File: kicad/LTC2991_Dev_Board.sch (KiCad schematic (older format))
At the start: 9 parts

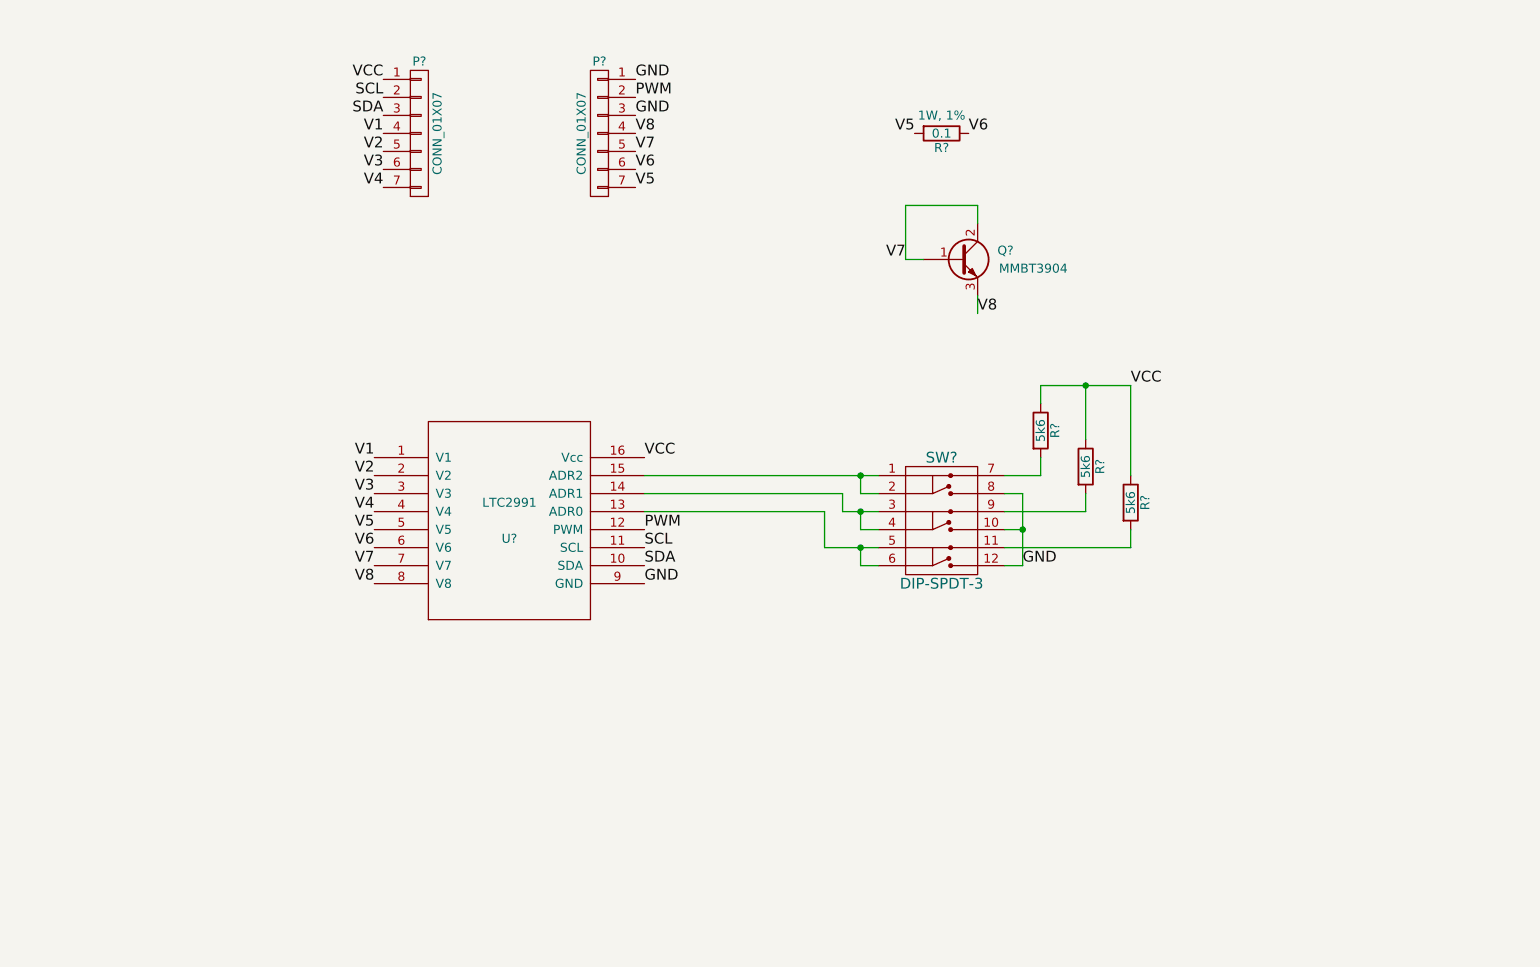
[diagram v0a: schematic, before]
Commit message: Beginning stages of PCB layout. Likely to need a few modifications to meet board size requirements.
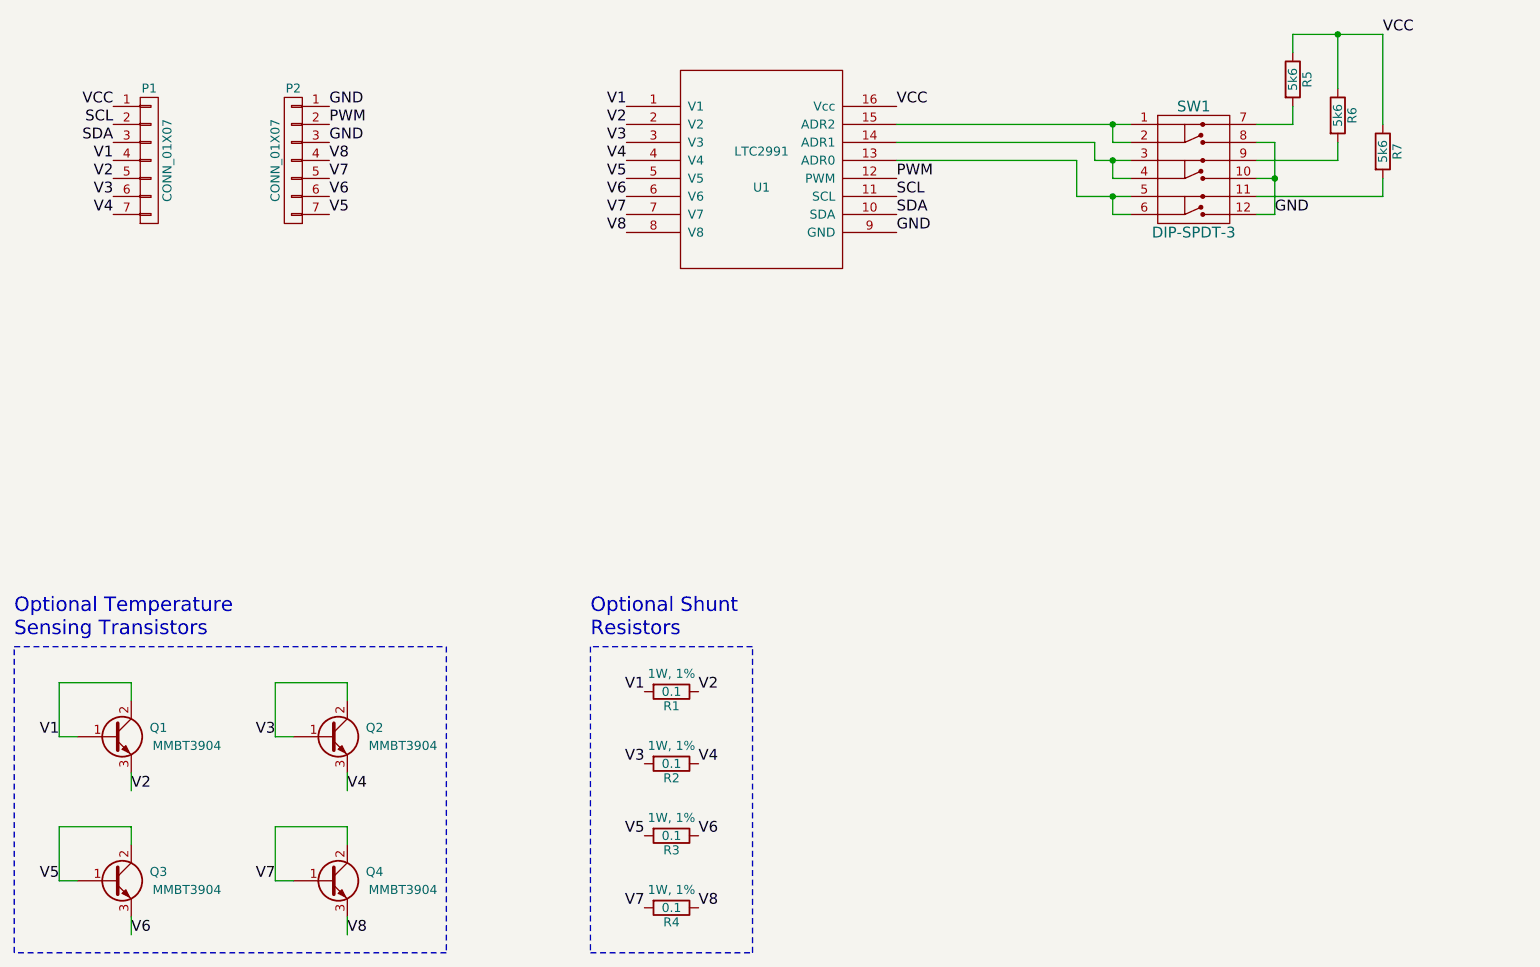
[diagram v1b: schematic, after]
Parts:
- added Q1, Q2, Q3: MMBT3904, Housings_SOT-23_SOT-143_TSOT-6:SOT-23, symbol Q_NPN_BCE
- added R2, R3, R4: 0.1, Resistors_SMD:R_2010, symbol R
- P1, P2: renamed from P?; footprint (none) -> Pin_Headers:Pin_Header_Straight_1x07
- Q4: renamed from Q?; footprint (none) -> Housings_SOT-23_SOT-143_TSOT-6:SOT-23
- R1: renamed from R?; footprint (none) -> Resistors_SMD:R_2010
- R5, R6, R7: renamed from R?; footprint (none) -> Resistors_SMD:R_1206
- SW1: renamed from SW?; footprint (none) -> Local:DIP_Switch_2x06
- U1: renamed from U?; footprint (none) -> Local:MSOP-16
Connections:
- net V1: now also R1.2, Q1.1 (B), Q1.2 (C)
- net V2: now also R1.1, Q1.3 (E)
- net V3: now also Q2.1 (B), Q2.2 (C), R2.2
- net V4: now also Q2.3 (E), R2.1
- net V5: now also Q3.1 (B), Q3.2 (C), R3.2; no longer R1.2
- net V6: now also Q3.3 (E), R3.1; no longer R1.1
- net V7: now also R4.2
- net V8: now also R4.1
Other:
- note added: "Optional Shunt\nResistors"
- note added: "Optional Temperature\nSensing Transistors"
- moved on the sheet: P1, P2, Q4, R1, R5, R6, R7, SW1, U1

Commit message: More PCB layout work, schematic tweaks. Closer to a finaly layout.
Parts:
- removed SW1: DIP-SPDT-3, Local:DIP_Switch_2x06, symbol DIP-SPDT-3
- added P3: CONN_02X03, Pin_Headers:Pin_Header_Straight_2x03, symbol CONN_02X03
- R1, R2, R3, R4: footprint Resistors_SMD:R_2010 -> Resistors_SMD:R_1206
- R5, R6, R7: footprint Resistors_SMD:R_1206 -> Resistors_SMD:R_0603
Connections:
- net GND: now also P3.1 (P1), P3.3 (P3), P3.5 (P5)
- net at U1.13 (ADR0): now also R7.2, P3.6 (P6)
- net at U1.14 (ADR1): now also R6.2, P3.4 (P4)
- net at U1.15 (ADR2): now also R5.2, P3.2 (P2)
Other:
- moved on the sheet: P1, P2, R5, R6, R7, U1
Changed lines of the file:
@@
 L LTC2991 U1
 U 1 1 55A19EC5
-P 5500 2950
-F 0 "U1" H 5500 2850 50  0000 C CNN
-F 1 "LTC2991" H 5500 3050 50  0000 C CNN
-F 2 "Local:MSOP-16" H 5500 2950 50  0001 C CNN
-F 3 "" H 5500 2950 50  0001 C CNN
-	1    5500 2950
-	1    0    0    -1
-$EndComp
-$Comp
-L DIP-SPDT-3 SW1
-U 1 1 55A1BC78
-P 7900 3200
-F 0 "SW1" H 7900 3800 60  0000 C CNN
-F 1 "DIP-SPDT-3" H 7900 3100 60  0000 C CNN
-F 2 "Local:DIP_Switch_2x06" H 7950 3200 60  0001 C CNN
-F 3 "" H 7950 3200 60  0000 C CNN
-	1    7900 3200
+P 5900 3300
+F 0 "U1" H 5900 3200 50  0000 C CNN
+F 1 "LTC2991" H 5900 3400 50  0000 C CNN
+F 2 "Local:MSOP-16" H 5900 3300 50  0001 C CNN
+F 3 "" H 5900 3300 50  0001 C CNN
+	1    5900 3300
 	1    0    0    -1
 $EndComp
@@
 L R R5
 U 1 1 55A1C08B
-P 8450 2450
-F 0 "R5" V 8530 2450 50  0000 C CNN
-F 1 "5k6" V 8450 2450 50  0000 C CNN
-F 2 "Resistors_SMD:R_1206" V 8380 2450 30  0001 C CNN
-F 3 "" H 8450 2450 30  0000 C CNN
-	1    8450 2450
+P 7600 2800
+F 0 "R5" V 7680 2800 50  0000 C CNN
+F 1 "5k6" V 7600 2800 50  0000 C CNN
+F 2 "Resistors_SMD:R_0603" V 7530 2800 30  0001 C CNN
+F 3 "" H 7600 2800 30  0000 C CNN
+	1    7600 2800
 	1    0    0    -1
 $EndComp
@@
 L R R6
 U 1 1 55A1C0C2
-P 8700 2650
-F 0 "R6" V 8780 2650 50  0000 C CNN
-F 1 "5k6" V 8700 2650 50  0000 C CNN
-F 2 "Resistors_SMD:R_1206" V 8630 2650 30  0001 C CNN
-F 3 "" H 8700 2650 30  0000 C CNN
-	1    8700 2650
+P 7850 2900
+F 0 "R6" V 7930 2900 50  0000 C CNN
+F 1 "5k6" V 7850 2900 50  0000 C CNN
+F 2 "Resistors_SMD:R_0603" V 7780 2900 30  0001 C CNN
+F 3 "" H 7850 2900 30  0000 C CNN
+	1    7850 2900
 	1    0    0    -1
 $EndComp
@@
 L R R7
 U 1 1 55A1C3A3
-P 8950 2850
-F 0 "R7" V 9030 2850 50  0000 C CNN
-F 1 "5k6" V 8950 2850 50  0000 C CNN
-F 2 "Resistors_SMD:R_1206" V 8880 2850 30  0001 C CNN
-F 3 "" H 8950 2850 30  0000 C CNN
-	1    8950 2850
-	1    0    0    -1
-$EndComp
-Text Label 8950 2200 0    60   ~ 0
+P 8100 3000
+F 0 "R7" V 8180 3000 50  0000 C CNN
+F 1 "5k6" V 8100 3000 50  0000 C CNN
+F 2 "Resistors_SMD:R_0603" V 8030 3000 30  0001 C CNN
+F 3 "" H 8100 3000 30  0000 C CNN
+	1    8100 3000
+	1    0    0    -1
+$EndComp
+Text Label 8100 2550 0    60   ~ 0
 VCC
-Text Label 6250 2600 0    60   ~ 0
+Text Label 6650 2950 0    60   ~ 0
 VCC
-Text Label 6250 3000 0    60   ~ 0
+Text Label 6650 3350 0    60   ~ 0
 PWM
-Text Label 6250 3100 0    60   ~ 0
+Text Label 6650 3450 0    60   ~ 0
 SCL
-Text Label 6250 3200 0    60   ~ 0
+Text Label 6650 3550 0    60   ~ 0
 SDA
-Text Label 4750 2600 2    60   ~ 0
+Text Label 5150 2950 2    60   ~ 0
 V1
-Text Label 4750 2700 2    60   ~ 0
+Text Label 5150 3050 2    60   ~ 0
 V2
-Text Label 4750 2800 2    60   ~ 0
+Text Label 5150 3150 2    60   ~ 0
 V3
-Text Label 4750 2900 2    60   ~ 0
+Text Label 5150 3250 2    60   ~ 0
 V4
-Text Label 1900 2600 2    60   ~ 0
+Text Label 2300 2950 2    60   ~ 0
 VCC
-Text Label 1900 2700 2    60   ~ 0
+Text Label 2300 3050 2    60   ~ 0
 SCL
-Text Label 1900 2800 2    60   ~ 0
+Text Label 2300 3150 2    60   ~ 0
 SDA
-Text Label 3100 2700 0    60   ~ 0
+Text Label 3500 3050 0    60   ~ 0
 PWM
-Text Label 1900 2900 2    60   ~ 0
+Text Label 2300 3250 2    60   ~ 0
 V1
-Text Label 1900 3000 2    60   ~ 0
+Text Label 2300 3350 2    60   ~ 0
 V2
-Text Label 1900 3100 2    60   ~ 0
+Text Label 2300 3450 2    60   ~ 0
 V3
-Text Label 1900 3200 2    60   ~ 0
+Text Label 2300 3550 2    60   ~ 0
 V4
-Text Label 3100 2600 0    60   ~ 0
+Text Label 3500 2950 0    60   ~ 0
 GND
-Text Label 6250 3300 0    60   ~ 0
-GND
-Text Label 8350 3200 0    60   ~ 0
+Text Label 6650 3650 0    60   ~ 0
 GND
 $Comp
@@
 F 0 "R1" V 5080 5850 50  0000 C CNN
 F 1 "0.1" V 5000 5850 50  0000 C CNN
-F 2 "Resistors_SMD:R_2010" V 4930 5850 30  0001 C CNN
+F 2 "Resistors_SMD:R_1206" V 4930 5850 30  0001 C CNN
 F 3 "" H 5000 5850 30  0000 C CNN
 F 4 "1W, 1%" V 4900 5850 50  0000 C CNN "Note"
@@
 $EndComp
 Wire Wire Line
-	6250 2700 7550 2700
-Wire Wire Line
-	7550 2800 7450 2800
-Wire Wire Line
-	7450 2800 7450 2700
-Connection ~ 7450 2700
-Wire Wire Line
-	6250 2800 7350 2800
-Wire Wire Line
-	7350 2800 7350 2900
-Wire Wire Line
-	7350 2900 7550 2900
-Wire Wire Line
-	7550 3000 7450 3000
-Wire Wire Line
-	7450 3000 7450 2900
-Connection ~ 7450 2900
-Wire Wire Line
-	6250 2900 7250 2900
-Wire Wire Line
-	7250 2900 7250 3100
-Wire Wire Line
-	7250 3100 7550 3100
-Wire Wire Line
-	7550 3200 7450 3200
-Wire Wire Line
-	7450 3200 7450 3100
-Connection ~ 7450 3100
-Wire Wire Line
-	8250 2700 8450 2700
-Wire Wire Line
-	8450 2700 8450 2600
-Wire Wire Line
-	8250 2900 8700 2900
-Wire Wire Line
-	8700 2900 8700 2800
-Wire Wire Line
-	8950 3000 8950 3100
-Wire Wire Line
-	8950 3100 8250 3100
-Wire Wire Line
-	8350 2800 8350 3200
-Wire Wire Line
-	8350 3200 8250 3200
-Wire Wire Line
-	8250 3000 8350 3000
-Wire Wire Line
-	8250 2800 8350 2800
-Connection ~ 8350 3000
-Wire Wire Line
-	8450 2200 8450 2300
-Wire Wire Line
-	8700 2500 8700 2200
-Wire Wire Line
-	8450 2200 8950 2200
-Wire Wire Line
-	8950 2200 8950 2700
-Connection ~ 8700 2200
-Text Label 4750 3000 2    60   ~ 0
+	7600 2950 7600 3500
+Wire Wire Line
+	7600 2550 7600 2650
+Wire Wire Line
+	7600 2550 8100 2550
+Connection ~ 7850 2550
+Text Label 5150 3350 2    60   ~ 0
 V5
-Text Label 4750 3100 2    60   ~ 0
+Text Label 5150 3450 2    60   ~ 0
 V6
-Text Label 4750 3200 2    60   ~ 0
+Text Label 5150 3550 2    60   ~ 0
 V7
-Text Label 4750 3300 2    60   ~ 0
+Text Label 5150 3650 2    60   ~ 0
 V8
 $Comp
 L CONN_01X07 P1
 U 1 1 55A22E52
-P 2100 2900
-F 0 "P1" H 2100 3300 50  0000 C CNN
-F 1 "CONN_01X07" V 2200 2900 50  0000 C CNN
-F 2 "Pin_Headers:Pin_Header_Straight_1x07" H 2100 2900 60  0001 C CNN
-F 3 "" H 2100 2900 60  0000 C CNN
-	1    2100 2900
+P 2500 3250
+F 0 "P1" H 2500 3650 50  0000 C CNN
+F 1 "CONN_01X07" V 2600 3250 50  0000 C CNN
+F 2 "Pin_Headers:Pin_Header_Straight_1x07" H 2500 3250 60  0001 C CNN
+F 3 "" H 2500 3250 60  0000 C CNN
+	1    2500 3250
 	1    0    0    -1
 $EndComp
@@
 L CONN_01X07 P2
 U 1 1 55A22EEE
-P 2900 2900
-F 0 "P2" H 2900 3300 50  0000 C CNN
-F 1 "CONN_01X07" V 3000 2900 50  0000 C CNN
-F 2 "Pin_Headers:Pin_Header_Straight_1x07" H 2900 2900 60  0001 C CNN
-F 3 "" H 2900 2900 60  0000 C CNN
-	1    2900 2900
+P 3300 3250
+F 0 "P2" H 3300 3650 50  0000 C CNN
+F 1 "CONN_01X07" V 3400 3250 50  0000 C CNN
+F 2 "Pin_Headers:Pin_Header_Straight_1x07" H 3300 3250 60  0001 C CNN
+F 3 "" H 3300 3250 60  0000 C CNN
+	1    3300 3250
 	-1   0    0    -1
 $EndComp
-Text Label 3100 3200 0    60   ~ 0
+Text Label 3500 3550 0    60   ~ 0
 V5
-Text Label 3100 3100 0    60   ~ 0
+Text Label 3500 3450 0    60   ~ 0
 V6
-Text Label 3100 3000 0    60   ~ 0
+Text Label 3500 3350 0    60   ~ 0
 V7
-Text Label 3100 2900 0    60   ~ 0
+Text Label 3500 3250 0    60   ~ 0
 V8
-Text Label 3100 2800 0    60   ~ 0
+Text Label 3500 3150 0    60   ~ 0
 GND
 Text Label 4850 5850 2    60   ~ 0
@@
 F 0 "R2" V 5080 6250 50  0000 C CNN
 F 1 "0.1" V 5000 6250 50  0000 C CNN
-F 2 "Resistors_SMD:R_2010" V 4930 6250 30  0001 C CNN
+F 2 "Resistors_SMD:R_1206" V 4930 6250 30  0001 C CNN
 F 3 "" H 5000 6250 30  0000 C CNN
 F 4 "1W, 1%" V 4900 6250 50  0000 C CNN "Note"
@@
 F 0 "R3" V 5080 6650 50  0000 C CNN
 F 1 "0.1" V 5000 6650 50  0000 C CNN
-F 2 "Resistors_SMD:R_2010" V 4930 6650 30  0001 C CNN
+F 2 "Resistors_SMD:R_1206" V 4930 6650 30  0001 C CNN
 F 3 "" H 5000 6650 30  0000 C CNN
 F 4 "1W, 1%" V 4900 6650 50  0000 C CNN "Note"
@@
 F 0 "R4" V 5080 7050 50  0000 C CNN
 F 1 "0.1" V 5000 7050 50  0000 C CNN
-F 2 "Resistors_SMD:R_2010" V 4930 7050 30  0001 C CNN
+F 2 "Resistors_SMD:R_1206" V 4930 7050 30  0001 C CNN
 F 3 "" H 5000 7050 30  0000 C CNN
 F 4 "1W, 1%" V 4900 7050 50  0000 C CNN "Note"
@@
 Text Notes 1350 5550 0    80   ~ 0
 Optional Temperature\nSensing Transistors
+$Comp
+L CONN_02X03 P3
+U 1 1 55A3F3AE
+P 7700 3750
+F 0 "P3" H 7700 3950 50  0000 C CNN
+F 1 "CONN_02X03" H 7700 3550 50  0000 C CNN
+F 2 "Pin_Headers:Pin_Header_Straight_2x03" H 7700 2550 60  0001 C CNN
+F 3 "" H 7700 2550 60  0000 C CNN
+	1    7700 3750
+	0    -1   -1   0
+$EndComp
+Wire Wire Line
+	7600 3050 6650 3050
+Wire Wire Line
+	7850 3050 7850 3350
+Wire Wire Line
+	7850 3150 6650 3150
+Wire Wire Line
+	8100 3150 8100 3400
+Wire Wire Line
+	8100 3250 6650 3250
+Wire Wire Line
+	7850 2750 7850 2550
+Wire Wire Line
+	8100 2550 8100 2850
+Connection ~ 7600 3050
+Wire Wire Line
+	7850 3350 7700 3350
+Wire Wire Line
+	7700 3350 7700 3500
+Connection ~ 7850 3150
+Wire Wire Line
+	8100 3400 7800 3400
+Wire Wire Line
+	7800 3400 7800 3500
+Connection ~ 8100 3250
+Wire Wire Line
+	7600 4000 7600 4100
+Wire Wire Line
+	7600 4100 7800 4100
+Wire Wire Line
+	7800 4100 7800 4000
+Wire Wire Line
+	7700 4000 7700 4100
+Connection ~ 7700 4100
+Text Label 7800 4100 0    60   ~ 0
+GND
 $EndSCHEMATC
